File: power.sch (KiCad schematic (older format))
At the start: 5 parts

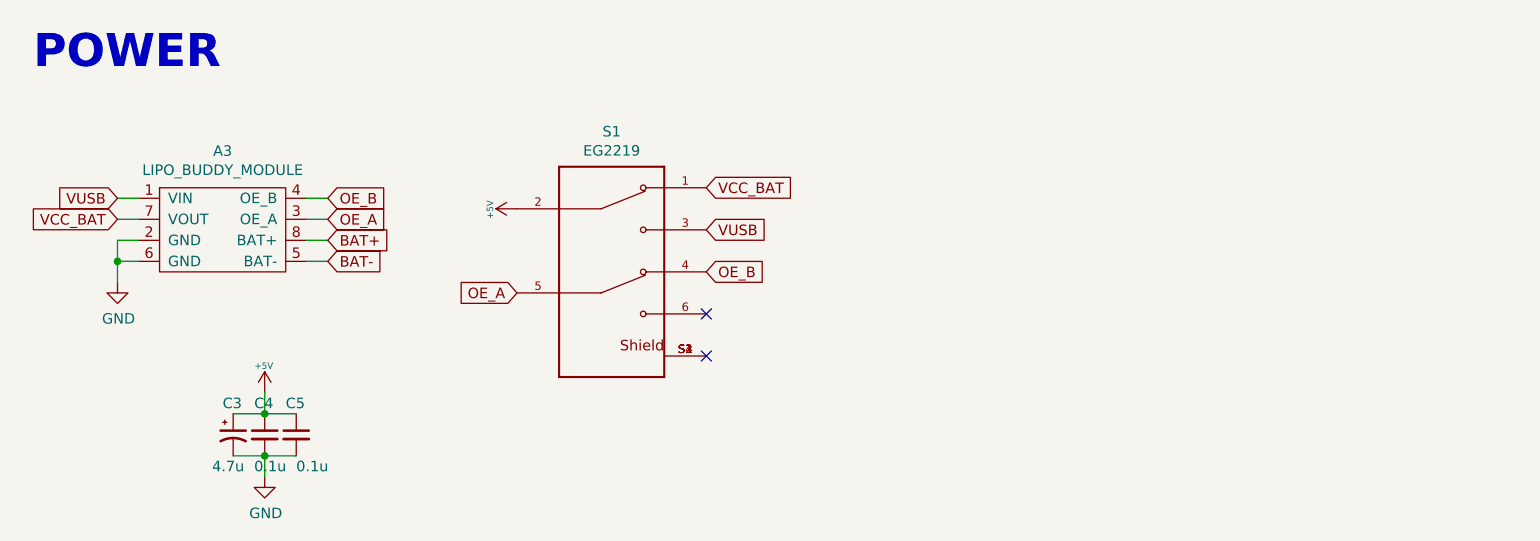
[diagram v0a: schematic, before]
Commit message: Add rotary encoder
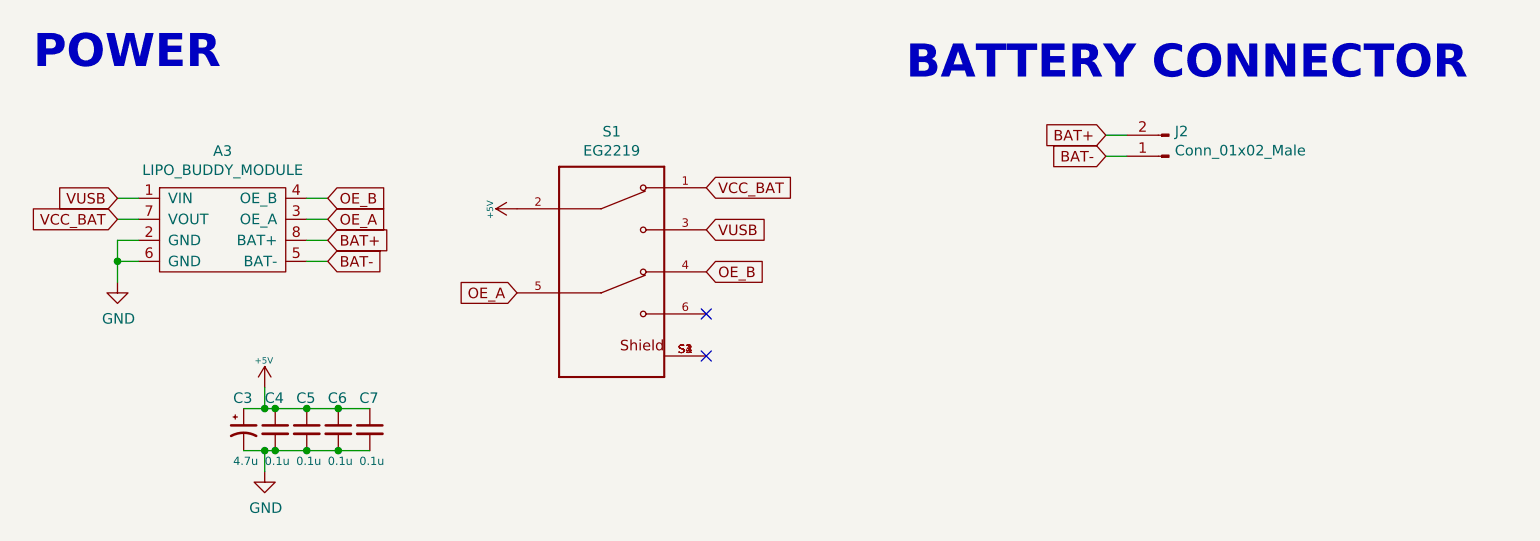
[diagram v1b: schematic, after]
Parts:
- added C6, C7: 0.1u, cftkb:C_Disc_D4.3mm_W1.9mm_P5.00mm, symbol Device:C_Small
- added J2: Conn_01x02_Male, Connector_JST:JST_PH_S2B-PH-K_1x02_P2.00mm_Horizontal, symbol Connector:Conn_01x02_Male
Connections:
- net +5V: now also C6.1, C7.1
- net BAT+: now also J2.2 (Pin_2)
- net BAT-: now also J2.1 (Pin_1)
- net GND: now also C6.2, C7.2
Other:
- note added: "BATTERY CONNECTOR\n"
- moved on the sheet: C3, C4, C5
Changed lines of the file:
@@
 L Device:CP1_Small C?
 U 1 1 5F370D30
-P 2050 3125
+P 2100 3100
 AR Path="/5F370D30" Ref="C?"  Part="1"
 AR Path="/5F36D657/5F370D30" Ref="C3"  Part="1"
-F 0 "C3" H 2000 3275 50  0000 L CNN
-F 1 "4.7u" H 1950 2975 50  0000 L CNN
-F 2 "cftkb:CP_Radial_D4.0mm_P1.50mm" H 2050 3125 50  0001 C CNN
-F 3 "~" H 2050 3125 50  0001 C CNN
-	1    2050 3125
-	1    0    0    -1
-$EndComp
-$Comp
-L Device:C_Small C?
-U 1 1 5F370D36
-P 2200 3125
-AR Path="/5F370D36" Ref="C?"  Part="1"
-AR Path="/5F36D657/5F370D36" Ref="C4"  Part="1"
-F 0 "C4" H 2150 3275 50  0000 L CNN
-F 1 "0.1u" H 2150 2975 50  0000 L CNN
-F 2 "cftkb:C_Disc_D4.3mm_W1.9mm_P5.00mm" H 2200 3125 50  0001 C CNN
-F 3 "~" H 2200 3125 50  0001 C CNN
-	1    2200 3125
+F 0 "C3" H 2050 3250 50  0000 L CNN
+F 1 "4.7u" H 2050 2950 39  0000 L CNN
+F 2 "cftkb:CP_Radial_D4.0mm_P1.50mm" H 2100 3100 50  0001 C CNN
+F 3 "~" H 2100 3100 50  0001 C CNN
+	1    2100 3100
 	1    0    0    -1
 $EndComp
@@
 L Device:C_Small C?
 U 1 1 5F370D3C
-P 2350 3125
+P 2400 3100
 AR Path="/5F370D3C" Ref="C?"  Part="1"
 AR Path="/5F36D657/5F370D3C" Ref="C5"  Part="1"
-F 0 "C5" H 2300 3275 50  0000 L CNN
-F 1 "0.1u" H 2350 2975 50  0000 L CNN
-F 2 "cftkb:C_Disc_D4.3mm_W1.9mm_P5.00mm" H 2350 3125 50  0001 C CNN
-F 3 "~" H 2350 3125 50  0001 C CNN
-	1    2350 3125
-	1    0    0    -1
-$EndComp
-Wire Wire Line
-	2050 3025 2200 3025
-Connection ~ 2200 3025
-Wire Wire Line
-	2200 3025 2350 3025
+F 0 "C5" H 2350 3250 50  0000 L CNN
+F 1 "0.1u" H 2350 2950 39  0000 L CNN
+F 2 "cftkb:C_Disc_D4.3mm_W1.9mm_P5.00mm" H 2400 3100 50  0001 C CNN
+F 3 "~" H 2400 3100 50  0001 C CNN
+	1    2400 3100
+	1    0    0    -1
+$EndComp
 $Comp
 L power:+5V #PWR?
 U 1 1 5F370D45
-P 2200 2925
+P 2200 2900
 AR Path="/5F370D45" Ref="#PWR?"  Part="1"
 AR Path="/5F36D657/5F370D45" Ref="#PWR0105"  Part="1"
-F 0 "#PWR0105" H 2200 3015 20  0001 C CNN
-F 1 "+5V" H 2196 3053 30  0000 C CNN
-F 2 "" H 2200 2925 60  0000 C CNN
-F 3 "" H 2200 2925 60  0000 C CNN
-	1    2200 2925
-	1    0    0    -1
-$EndComp
-Wire Wire Line
-	2200 3025 2200 2925
-Wire Wire Line
-	2050 3225 2200 3225
-Connection ~ 2200 3225
-Wire Wire Line
-	2200 3225 2350 3225
-Wire Wire Line
-	2200 3225 2200 3325
-$Comp
-L power:GND #PWR?
-U 1 1 5F370D50
-P 2200 3325
-AR Path="/5F370D50" Ref="#PWR?"  Part="1"
-AR Path="/5F36D657/5F370D50" Ref="#PWR0111"  Part="1"
-F 0 "#PWR0111" H 2200 3075 50  0001 C CNN
-F 1 "GND" H 2205 3152 50  0000 C CNN
-F 2 "" H 2200 3325 50  0001 C CNN
-F 3 "" H 2200 3325 50  0001 C CNN
-	1    2200 3325
+F 0 "#PWR0105" H 2200 2990 20  0001 C CNN
+F 1 "+5V" H 2196 3028 30  0000 C CNN
+F 2 "" H 2200 2900 60  0000 C CNN
+F 3 "" H 2200 2900 60  0000 C CNN
+	1    2200 2900
 	1    0    0    -1
 $EndComp
@@
 $EndComp
 NoConn ~ 4300 2750
+$Comp
+L Device:C_Small C?
+U 1 1 5F370D36
+P 2250 3100
+AR Path="/5F370D36" Ref="C?"  Part="1"
+AR Path="/5F36D657/5F370D36" Ref="C4"  Part="1"
+F 0 "C4" H 2200 3250 50  0000 L CNN
+F 1 "0.1u" H 2200 2950 39  0000 L CNN
+F 2 "cftkb:C_Disc_D4.3mm_W1.9mm_P5.00mm" H 2250 3100 50  0001 C CNN
+F 3 "~" H 2250 3100 50  0001 C CNN
+	1    2250 3100
+	1    0    0    -1
+$EndComp
+$Comp
+L power:GND #PWR?
+U 1 1 5F370D50
+P 2200 3300
+AR Path="/5F370D50" Ref="#PWR?"  Part="1"
+AR Path="/5F36D657/5F370D50" Ref="#PWR0111"  Part="1"
+F 0 "#PWR0111" H 2200 3050 50  0001 C CNN
+F 1 "GND" H 2205 3127 50  0000 C CNN
+F 2 "" H 2200 3300 50  0001 C CNN
+F 3 "" H 2200 3300 50  0001 C CNN
+	1    2200 3300
+	1    0    0    -1
+$EndComp
+$Comp
+L Device:C_Small C?
+U 1 1 5F3B0936
+P 2550 3100
+AR Path="/5F3B0936" Ref="C?"  Part="1"
+AR Path="/5F36D657/5F3B0936" Ref="C6"  Part="1"
+F 0 "C6" H 2500 3250 50  0000 L CNN
+F 1 "0.1u" H 2500 2950 39  0000 L CNN
+F 2 "cftkb:C_Disc_D4.3mm_W1.9mm_P5.00mm" H 2550 3100 50  0001 C CNN
+F 3 "~" H 2550 3100 50  0001 C CNN
+	1    2550 3100
+	1    0    0    -1
+$EndComp
+$Comp
+L Device:C_Small C?
+U 1 1 5F3B0AB2
+P 2700 3100
+AR Path="/5F3B0AB2" Ref="C?"  Part="1"
+AR Path="/5F36D657/5F3B0AB2" Ref="C7"  Part="1"
+F 0 "C7" H 2650 3250 50  0000 L CNN
+F 1 "0.1u" H 2650 2950 39  0000 L CNN
+F 2 "cftkb:C_Disc_D4.3mm_W1.9mm_P5.00mm" H 2700 3100 50  0001 C CNN
+F 3 "~" H 2700 3100 50  0001 C CNN
+	1    2700 3100
+	1    0    0    -1
+$EndComp
+Wire Wire Line
+	2100 3200 2200 3200
+Connection ~ 2250 3200
+Wire Wire Line
+	2250 3200 2400 3200
+Connection ~ 2400 3200
+Wire Wire Line
+	2400 3200 2550 3200
+Connection ~ 2550 3200
+Wire Wire Line
+	2550 3200 2700 3200
+Wire Wire Line
+	2100 3000 2200 3000
+Connection ~ 2250 3000
+Wire Wire Line
+	2250 3000 2400 3000
+Connection ~ 2400 3000
+Wire Wire Line
+	2400 3000 2550 3000
+Connection ~ 2550 3000
+Wire Wire Line
+	2550 3000 2700 3000
+Wire Wire Line
+	2200 2900 2200 3000
+Connection ~ 2200 3000
+Wire Wire Line
+	2200 3000 2250 3000
+Wire Wire Line
+	2200 3300 2200 3200
+Connection ~ 2200 3200
+Wire Wire Line
+	2200 3200 2250 3200
+Text Notes 5250 1450 0    157  ~ 31
+BATTERY CONNECTOR\n
+$Comp
+L Connector:Conn_01x02_Male J2
+U 1 1 5F537CC3
+P 6500 1800
+F 0 "J2" H 6472 1682 50  0000 R CNN
+F 1 "Conn_01x02_Male" H 6472 1773 50  0000 R CNN
+F 2 "Connector_JST:JST_PH_S2B-PH-K_1x02_P2.00mm_Horizontal" H 6500 1800 50  0001 C CNN
+F 3 "~" H 6500 1800 50  0001 C CNN
+	1    6500 1800
+	-1   0    0    1
+$EndComp
+Text GLabel 6200 1800 0    50   Input ~ 0
+BAT-
+Text GLabel 6200 1700 0    50   Input ~ 0
+BAT+
+Wire Wire Line
+	6200 1700 6300 1700
+Wire Wire Line
+	6200 1800 6300 1800
 $EndSCHEMATC
